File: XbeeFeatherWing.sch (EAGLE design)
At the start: 18 parts, among them U2 XBEE-1B3

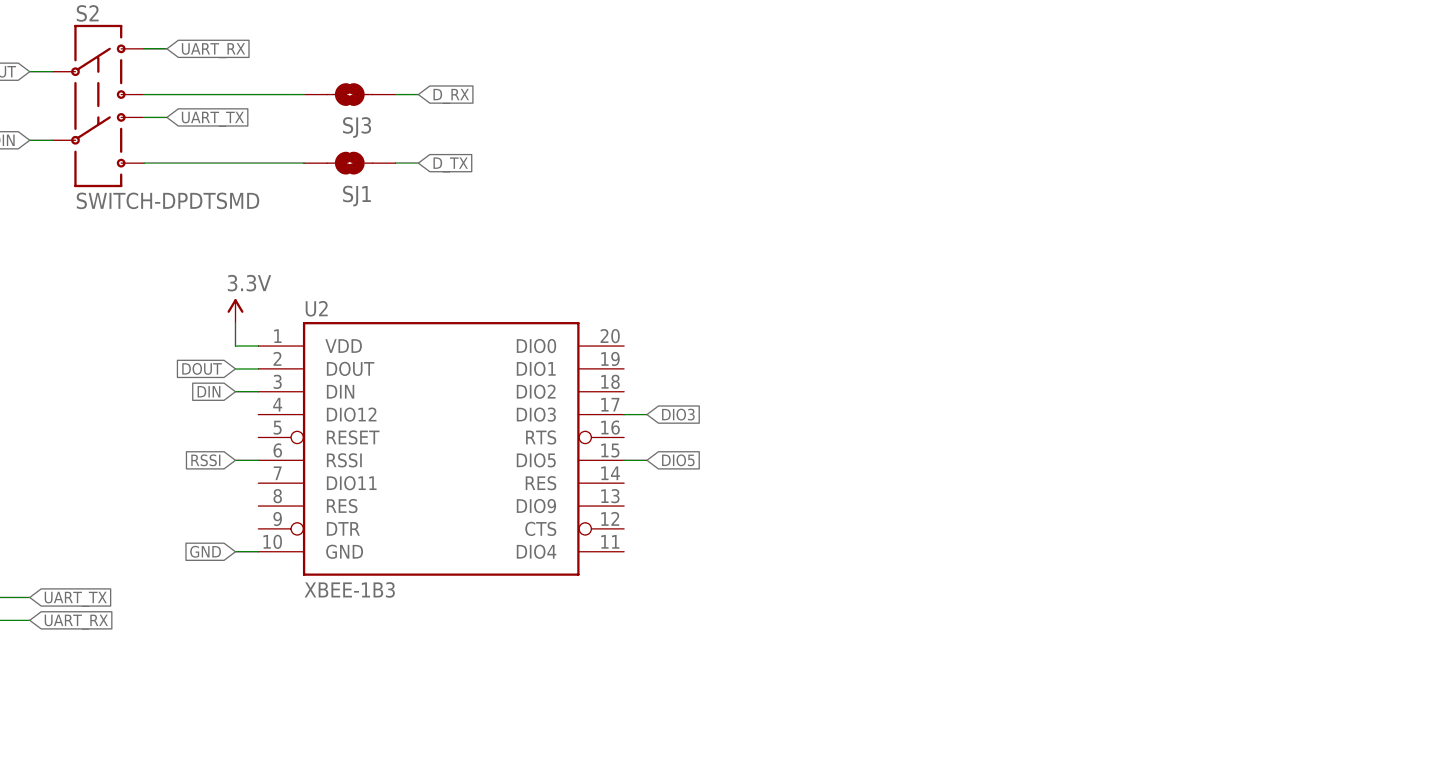
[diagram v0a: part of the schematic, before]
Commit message: changed xbee to adafruit footprint
the sparkfun footprint was smd, needed THT pins
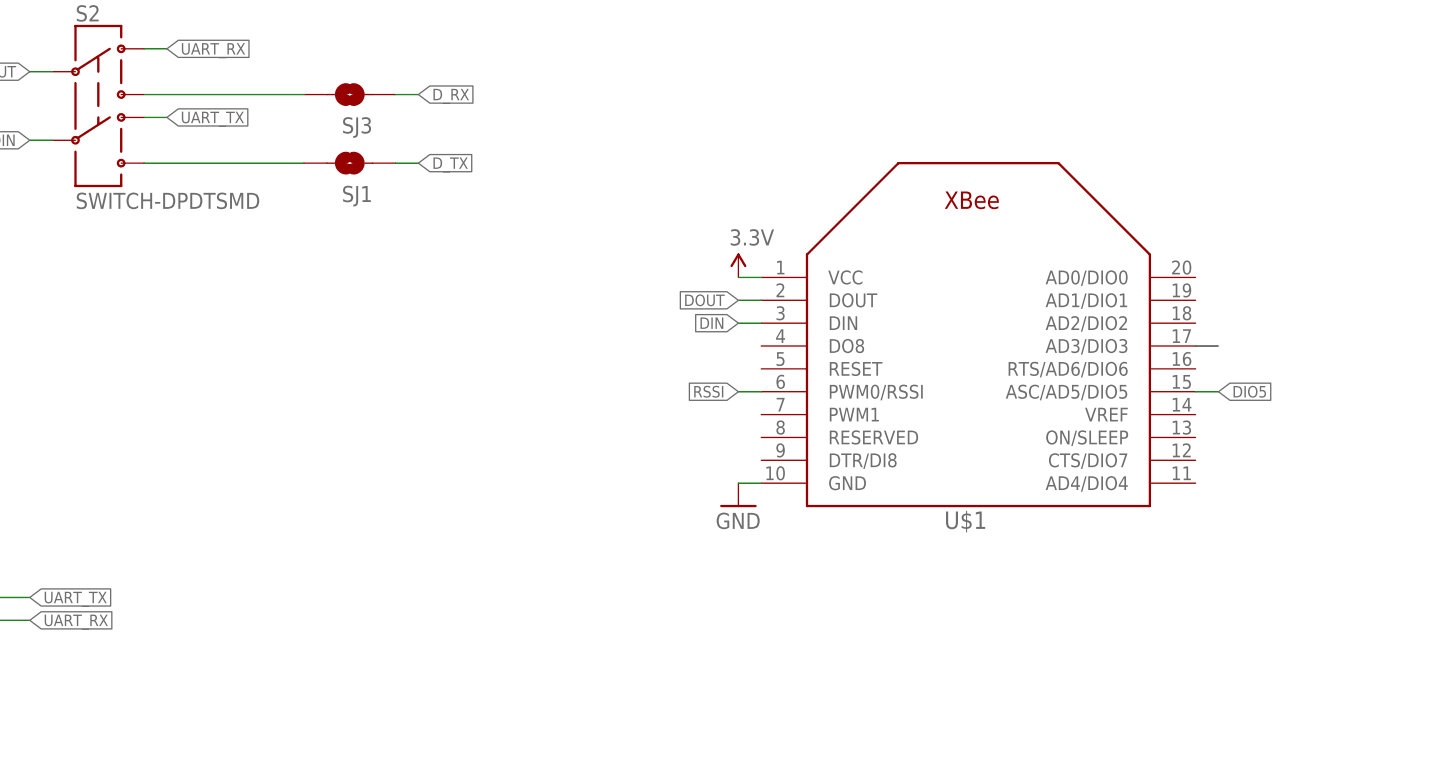
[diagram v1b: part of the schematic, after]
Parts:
- removed U2: XBEE-1B3, SparkFun:XBEE-1B3
- added U$1: XBEE, adafruit:XBEE
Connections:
- new net N$8: U$1.AD3/DIO3
- net 3.3V: now also U$1.VCC; no longer U2.VDD
- net DIN: now also U$1.DIN; no longer U2.DIN
- net DIO3: no longer U2.DIO3
- net DIO5: now also U$1.ASC/AD5/DIO5; no longer U2.DIO5
- net DOUT: now also U$1.DOUT; no longer U2.DOUT
- net GND: now also U$1.GND; no longer U2.GND
- net RSSI: now also U$1.PWM0/RSSI; no longer U2.RSSI
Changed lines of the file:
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@@
 <part name="R1" library="SparkFun-Resistors" deviceset="1KOHM1/10W1%(0603)" device="" value="1k"/>
 <part name="R3" library="SparkFun-Resistors" deviceset="1KOHM1/10W1%(0603)" device="" value="1k"/>
-<part name="U2" library="SparkFun" deviceset="XBEE-1" device="B3"/>
-<part name="P+1" library="SparkFun" deviceset="3.3V" device=""/>
 <part name="LED4" library="SparkFun-LED" deviceset="LED-GREEN" device="0603" value="Green"/>
 <part name="R4" library="SparkFun-Resistors" deviceset="1KOHM1/10W1%(0603)" device="" value="1k"/>
@@
 <part name="GND7" library="SparkFun" deviceset="GND" device=""/>
 <part name="P+8" library="SparkFun" deviceset="3.3V" device=""/>
+<part name="U$1" library="adafruit" deviceset="XBEE" device=""/>
+<part name="P+5" library="SparkFun" deviceset="3.3V" device=""/>
+<part name="GND1" library="SparkFun" deviceset="GND" device=""/>
 </parts>
 <sheets>
@@
 <instance part="R1" gate="G$1" x="10.16" y="167.64" rot="R270"/>
 <instance part="R3" gate="G$1" x="20.32" y="167.64" rot="R270"/>
-<instance part="U2" gate="G$1" x="127" y="134.62"/>
-<instance part="P+1" gate="G$1" x="104.14" y="147.32"/>
 <instance part="LED4" gate="G$1" x="33.02" y="157.48"/>
 <instance part="R4" gate="G$1" x="33.02" y="167.64" rot="R90"/>
@@
 <instance part="GND7" gate="1" x="81.28" y="88.9" rot="R90"/>
 <instance part="P+8" gate="G$1" x="86.36" y="91.44"/>
+<instance part="U$1" gate="G$1" x="185.42" y="142.24"/>
+<instance part="P+5" gate="G$1" x="160.02" y="152.4"/>
+<instance part="GND1" gate="1" x="160.02" y="127"/>
 </instances>
 <busses>
@@
 </segment>
 <segment>
-<wire x1="106.68" y1="121.92" x2="104.14" y2="121.92" width="0.1524" layer="91"/>
-<label x="104.14" y="121.92" size="1.27" layer="95" rot="R180" xref="yes"/>
-<pinref part="U2" gate="G$1" pin="GND"/>
+<pinref part="U$1" gate="G$1" pin="GND"/>
+<wire x1="162.56" y1="129.54" x2="160.02" y2="129.54" width="0.1524" layer="91"/>
+<pinref part="GND1" gate="1" pin="GND"/>
 </segment>
 </net>
@@
 </segment>
 <segment>
-<pinref part="U2" gate="G$1" pin="DIN"/>
-<wire x1="106.68" y1="139.7" x2="104.14" y2="139.7" width="0.1524" layer="91"/>
-<label x="104.14" y="139.7" size="1.27" layer="95" rot="R180" xref="yes"/>
-</segment>
-<segment>
 <wire x1="83.82" y1="167.64" x2="81.28" y2="167.64" width="0.1524" layer="91"/>
 <pinref part="S2" gate="G$1" pin="5"/>
 <label x="81.28" y="167.64" size="1.27" layer="95" rot="R180" xref="yes"/>
 </segment>
+<segment>
+<pinref part="U$1" gate="G$1" pin="DIN"/>
+<wire x1="162.56" y1="147.32" x2="160.02" y2="147.32" width="0.1524" layer="91"/>
+<label x="160.02" y="147.32" size="1.27" layer="95" rot="R180" xref="yes"/>
+</segment>
 </net>
 <net name="DOUT" class="0">
@@
 </segment>
 <segment>
-<pinref part="U2" gate="G$1" pin="DOUT"/>
-<wire x1="106.68" y1="142.24" x2="104.14" y2="142.24" width="0.1524" layer="91"/>
-<label x="104.14" y="142.24" size="1.27" layer="95" rot="R180" xref="yes"/>
-</segment>
-<segment>
 <wire x1="83.82" y1="175.26" x2="81.28" y2="175.26" width="0.1524" layer="91"/>
 <pinref part="S2" gate="G$1" pin="2"/>
 <label x="81.28" y="175.26" size="1.27" layer="95" rot="R180" xref="yes"/>
 </segment>
+<segment>
+<pinref part="U$1" gate="G$1" pin="DOUT"/>
+<wire x1="162.56" y1="149.86" x2="160.02" y2="149.86" width="0.1524" layer="91"/>
+<label x="160.02" y="149.86" size="1.27" layer="95" rot="R180" xref="yes"/>
+</segment>
 </net>
 <net name="3.3V" class="0">
-<segment>
-<wire x1="106.68" y1="144.78" x2="104.14" y2="144.78" width="0.1524" layer="91"/>
-<wire x1="104.14" y1="144.78" x2="104.14" y2="147.32" width="0.1524" layer="91"/>
-<pinref part="U2" gate="G$1" pin="VDD"/>
-<pinref part="P+1" gate="G$1" pin="3.3V"/>
-</segment>
 <segment>
 <wire x1="45.72" y1="175.26" x2="45.72" y2="172.72" width="0.1524" layer="91"/>
@@
 <wire x1="86.36" y1="83.82" x2="76.2" y2="83.82" width="0.1524" layer="91"/>
 </segment>
+<segment>
+<pinref part="U$1" gate="G$1" pin="VCC"/>
+<wire x1="162.56" y1="152.4" x2="160.02" y2="152.4" width="0.1524" layer="91"/>
+<pinref part="P+5" gate="G$1" pin="3.3V"/>
+</segment>
 </net>
 <net name="DIO5" class="0">
-<segment>
-<wire x1="149.86" y1="132.08" x2="147.32" y2="132.08" width="0.1524" layer="91"/>
-<label x="149.86" y="132.08" size="1.27" layer="95" xref="yes"/>
-<pinref part="U2" gate="G$1" pin="DIO5"/>
-</segment>
 <segment>
 <wire x1="60.96" y1="172.72" x2="60.96" y2="175.26" width="0.1524" layer="91"/>
@@
 <label x="60.96" y="175.26" size="1.27" layer="95" rot="R90" xref="yes"/>
 </segment>
+<segment>
+<pinref part="U$1" gate="G$1" pin="ASC/AD5/DIO5"/>
+<wire x1="210.82" y1="139.7" x2="213.36" y2="139.7" width="0.1524" layer="91"/>
+<label x="213.36" y="139.7" size="1.27" layer="95" xref="yes"/>
+</segment>
 </net>
 <net name="DIO3" class="0">
-<segment>
-<wire x1="149.86" y1="137.16" x2="147.32" y2="137.16" width="0.1524" layer="91"/>
-<label x="149.86" y="137.16" size="1.27" layer="95" xref="yes"/>
-<pinref part="U2" gate="G$1" pin="DIO3"/>
-</segment>
 <segment>
 <wire x1="12.7" y1="119.38" x2="12.7" y2="127" width="0.1524" layer="91"/>
@@
 <net name="RSSI" class="0">
 <segment>
-<wire x1="106.68" y1="132.08" x2="104.14" y2="132.08" width="0.1524" layer="91"/>
-<label x="104.14" y="132.08" size="1.27" layer="95" rot="R180" xref="yes"/>
-<pinref part="U2" gate="G$1" pin="RSSI"/>
-</segment>
-<segment>
 <wire x1="33.02" y1="172.72" x2="33.02" y2="175.26" width="0.1524" layer="91"/>
 <pinref part="R4" gate="G$1" pin="2"/>
 <label x="33.02" y="175.26" size="1.27" layer="95" rot="R90" xref="yes"/>
+</segment>
+<segment>
+<pinref part="U$1" gate="G$1" pin="PWM0/RSSI"/>
+<wire x1="162.56" y1="139.7" x2="160.02" y2="139.7" width="0.1524" layer="91"/>
+<label x="160.02" y="139.7" size="1.27" layer="95" rot="R180" xref="yes"/>
 </segment>
 </net>
@@
 </segment>
 </net>
+<net name="N$8" class="0">
+<segment>
+<pinref part="U$1" gate="G$1" pin="AD3/DIO3"/>
+<wire x1="210.82" y1="144.78" x2="213.36" y2="144.78" width="0.1524" layer="91"/>
+</segment>
+</net>

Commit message: v1 of the board with layout complete
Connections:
- removed net N$8: U$1.AD3/DIO3
- net DIO3: now also U$1.AD3/DIO3
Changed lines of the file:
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@@
 <attribute name="NAME" x="86.36" y="78.74" size="1.778" layer="95" rot="R180"/>
 </instance>
-<instance part="GND8" gate="1" x="93.98" y="81.28" rot="R90"/>
+<instance part="GND8" gate="1" x="99.06" y="81.28" rot="R90"/>
 <instance part="SJ2" gate="1" x="12.7" y="114.3" rot="R90"/>
 <instance part="C4" gate="G$1" x="12.7" y="96.52" rot="R180"/>
@@
 </segment>
 <segment>
-<wire x1="88.9" y1="81.28" x2="91.44" y2="81.28" width="0.1524" layer="91"/>
+<wire x1="88.9" y1="81.28" x2="96.52" y2="81.28" width="0.1524" layer="91"/>
 <pinref part="S1" gate="G$1" pin="1"/>
 <pinref part="GND8" gate="1" pin="GND"/>
@@
 <label x="12.7" y="127" size="1.27" layer="95" rot="R90" xref="yes"/>
 </segment>
+<segment>
+<pinref part="U$1" gate="G$1" pin="AD3/DIO3"/>
+<wire x1="210.82" y1="144.78" x2="213.36" y2="144.78" width="0.1524" layer="91"/>
+<label x="213.36" y="144.78" size="1.27" layer="95" xref="yes"/>
+</segment>
 </net>
 <net name="RSSI" class="0">
@@
 </segment>
 </net>
-<net name="N$8" class="0">
-<segment>
-<pinref part="U$1" gate="G$1" pin="AD3/DIO3"/>
-<wire x1="210.82" y1="144.78" x2="213.36" y2="144.78" width="0.1524" layer="91"/>
-</segment>
-</net>

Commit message: routing complete
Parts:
- SJ2: value SOLDERJUMPERTRACE -> SOLDERJUMPERNC; device SparkFun:SOLDERJUMPERTRACE -> SparkFun-Retired:SOLDERJUMPERNC
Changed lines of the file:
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@@
 <part name="S1" library="SparkFun" deviceset="SWITCH-MOMENTARY-2" device="SMD"/>
 <part name="GND8" library="SparkFun" deviceset="GND" device=""/>
-<part name="SJ2" library="SparkFun" deviceset="SOLDERJUMPER" device="TRACE"/>
+<part name="SJ2" library="SparkFun-Retired" deviceset="SOLDERJUMPER" device="NC"/>
 <part name="C4" library="SparkFun-Capacitors" deviceset="0.1UF-25V(+80/-20%)(0603)" device="" value="0.1uF"/>
 <part name="LED5" library="SparkFun-LED" deviceset="LED-GREEN" device="0603" value="Green"/>
